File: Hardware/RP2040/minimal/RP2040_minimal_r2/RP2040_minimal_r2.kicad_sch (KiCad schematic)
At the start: 27 parts, among them J3 Conn_02x18_Odd_Even, J4 Conn_02x18_Odd_Even, SW1 TL3342F160QG_TR, U2 W25Q128JVS, U3 RP2040, Y1 12Mhz

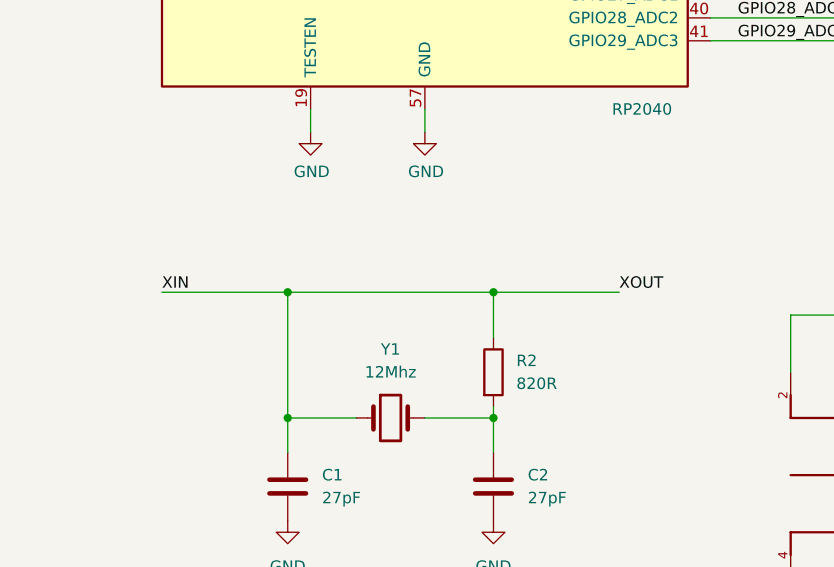
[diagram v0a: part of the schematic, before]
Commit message: some more BMS work + fixed RP2040 XIN/XOUT shortage
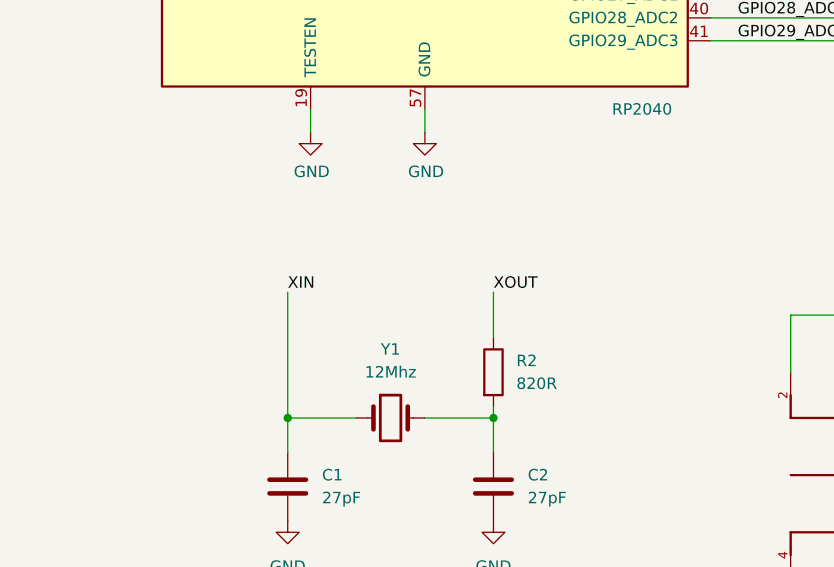
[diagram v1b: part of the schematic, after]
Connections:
- net XIN: no longer R2.1, U3.21 (XOUT)
- new net XOUT: R2.1, U3.21 (XOUT)
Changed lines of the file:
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@@
 	)
 	(junction
-		(at 48.26 237.49)
-		(diameter 0)
-		(color 0 0 0 0)
-	)
-	(junction
 		(at 224.79 189.23)
 		(diameter 0)
@@
 	)
 	(junction
-		(at 71.12 237.49)
-		(diameter 0)
-		(color 0 0 0 0)
-	)
-	(junction
 		(at 62.23 102.87)
 		(diameter 0)
@@
 	(wire
 		(pts
-			(xy 71.12 237.49) (xy 85.09 237.49)
-		)
-		(stroke
-			(width 0)
-			(type default)
-		)
-	)
-	(wire
-		(pts
 			(xy 95.25 186.69) (xy 110.49 186.69)
 		)
@@
 	(wire
 		(pts
-			(xy 48.26 237.49) (xy 71.12 237.49)
-		)
-		(stroke
-			(width 0)
-			(type default)
-		)
-	)
-	(wire
-		(pts
 			(xy 88.9 83.82) (xy 88.9 82.55)
 		)
@@
 	(wire
 		(pts
-			(xy 34.29 237.49) (xy 48.26 237.49)
-		)
-		(stroke
-			(width 0)
-			(type default)
-		)
-	)
-	(wire
-		(pts
 			(xy 153.67 168.91) (xy 152.4 168.91)
 		)
@@
 	)
 	(label "XIN"
-		(at 34.29 237.49 0)
+		(at 48.26 237.49 0)
 		(effects
 			(font
@@
 	)
 	(label "XOUT"
-		(at 85.09 237.49 0)
+		(at 71.12 237.49 0)
 		(effects
 			(font
